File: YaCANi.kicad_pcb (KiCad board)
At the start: 2 copper layers, 20 x 50 mm, 62 parts, among them P1 SWD, P2 CAN, P3 USB, U1 STM32F042C6T6, U2 MCP2562-E/SN, U3 LD1117S33TR

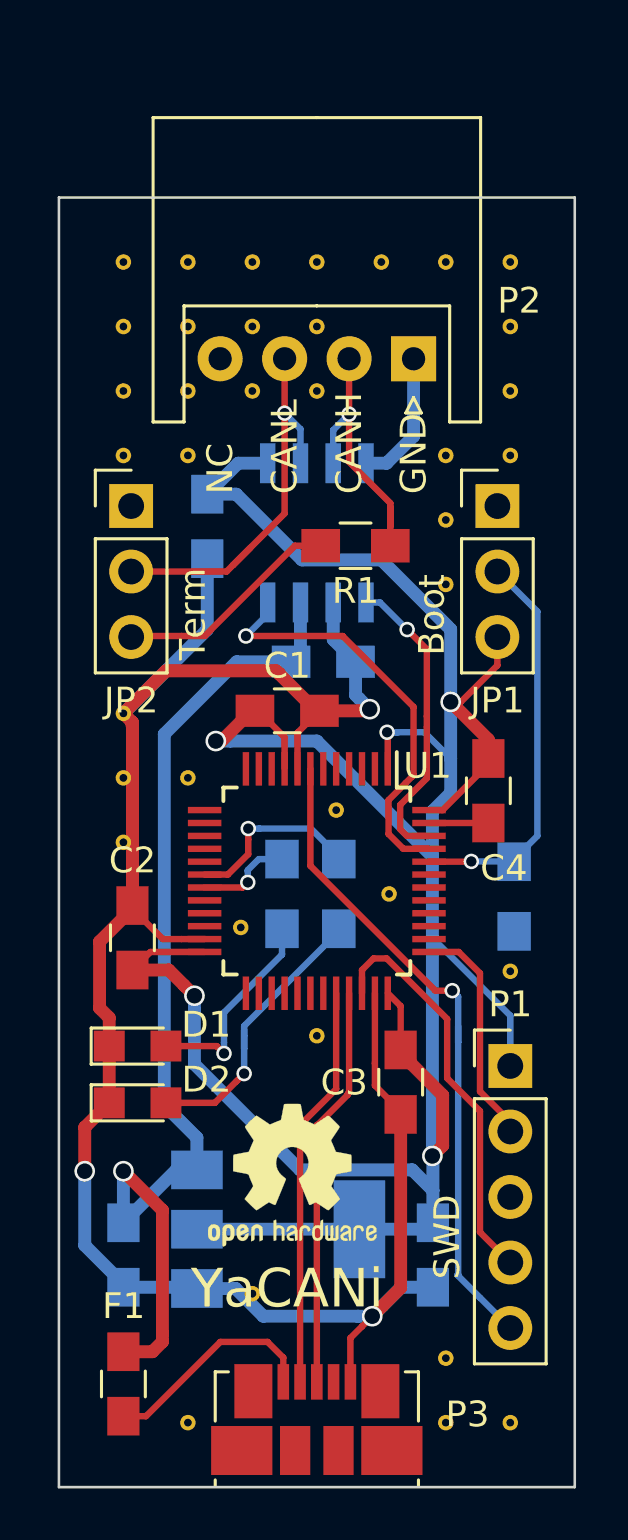
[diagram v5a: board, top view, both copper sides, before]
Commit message: add LED labelling
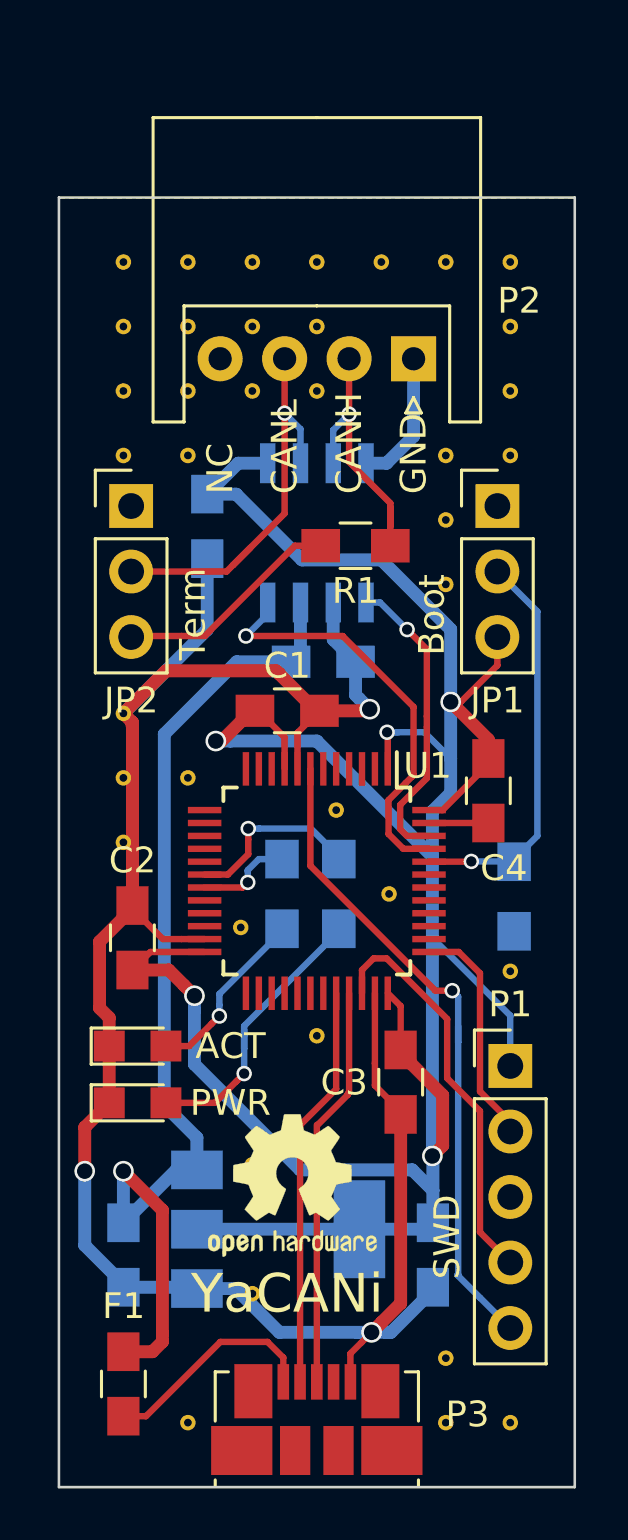
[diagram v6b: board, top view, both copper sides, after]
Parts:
- moved REF*** 0.40 mm to (130.8, 115.8)
- renumbered D1 to ACT, D2 to PWR
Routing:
- net Net-(D1-Pad2): track 8.14 -> 6.94 mm
- net GND: track 97.0 -> 97.6 mm
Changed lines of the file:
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@@
     (thickness 1.6)
     (drawings 20)
-    (tracks 280)
+    (tracks 282)
     (zones 0)
     (modules 62)
@@
     (tags "LED led 0805 SMD smd SMT smt smdled SMDLED smtled SMTLED")
     (attr smd)
-    (fp_text reference D1 (at 2.66 -0.83) (layer F.SilkS)
+    (fp_text reference ACT (at 3.6 0) (layer F.SilkS)
       (effects (font (size 1 1) (thickness 0.15)))
     )
@@
     (tags "LED led 0805 SMD smd SMT smt smdled SMDLED smtled SMTLED")
     (attr smd)
-    (fp_text reference D2 (at 2.67 -0.9) (layer F.SilkS)
+    (fp_text reference PWR (at 3.6 0) (layer F.SilkS)
       (effects (font (size 1 1) (thickness 0.15)))
     )
@@
   )
   (module Symbols:OSHW-Logo2_7.3x6mm_SilkScreen (layer F.Cu)
-    (at 130.8 115.4)
+    (at 130.8 115.8)
     (descr "Open Source Hardware Symbol")
     (tags "Logo Symbol OSHW")
@@
       (xy -0.113933 -2.757629) (xy -0.013056 -2.757714) (xy 0 -2.757714) (xy 0.10391 -2.757652)) (layer F.SilkS) (width 0.01))
   )
-  (gr_text YaCANi (at 130.6 119.8 360) (layer F.SilkS)
+  (gr_text YaCANi (at 130.6 120 360) (layer F.SilkS)
     (effects (font (size 1.5 1.5) (thickness 0.3)))
   )
@@
     (arrow2b (pts (xy 121.75 72.5) (xy 122.876504 71.913579)))
   )
+  (segment (start 136.25 119.875) (end 134.626021 121.498979) (width 0.5) (layer B.Cu) (net 1))
+  (segment (start 135 120.373239) (end 134.274259 121.09898) (width 0.5) (layer F.Cu) (net 1))
+  (segment (start 133.474261 121.898978) (end 133.87426 121.498979) (width 0.25) (layer F.Cu) (net 1))
+  (segment (start 135 113.05) (end 135 120.373239) (width 0.5) (layer F.Cu) (net 1))
+  (segment (start 133.05 122.323239) (end 133.474261 121.898978) (width 0.25) (layer F.Cu) (net 1))
+  (segment (start 133.05 123.42) (end 133.05 122.323239) (width 0.25) (layer F.Cu) (net 1))
+  (segment (start 134.439945 121.498979) (end 133.87426 121.498979) (width 0.5) (layer B.Cu) (net 1))
+  (segment (start 136.25 119.75) (end 136.25 119.875) (width 0.5) (layer B.Cu) (net 1))
+  (segment (start 134.274259 121.09898) (end 133.87426 121.498979) (width 0.5) (layer F.Cu) (net 1))
+  (segment (start 133.308575 121.498979) (end 133.87426 121.498979) (width 0.5) (layer B.Cu) (net 1))
+  (segment (start 130.298979 121.498979) (end 133.308575 121.498979) (width 0.5) (layer B.Cu) (net 1))
+  (segment (start 127.1 119.8) (end 128.6 119.8) (width 0.5) (layer B.Cu) (net 1))
+  (segment (start 134.626021 121.498979) (end 134.439945 121.498979) (width 0.5) (layer B.Cu) (net 1))
+  (via (at 133.87426 121.498979) (size 0.8) (drill 0.6) (layers F.Cu B.Cu) (net 1))
+  (segment (start 128.6 119.8) (end 130.298979 121.498979) (width 0.5) (layer B.Cu) (net 1))
   (segment (start 136.1 101.75) (end 138.4 101.75) (width 0.25) (layer F.Cu) (net 1))
   (segment (start 135.5 86.755) (end 135.5 83.75) (width 0.5) (layer B.Cu) (net 1))
@@
   (segment (start 135.5 86.755) (end 134.455 87.8) (width 0.5) (layer B.Cu) (net 1))
   (segment (start 134.455 87.8) (end 133.655 87.8) (width 0.5) (layer B.Cu) (net 1))
-  (segment (start 133.497956 121.272711) (end 133.897955 120.872712) (width 0.25) (layer F.Cu) (net 1))
-  (segment (start 133.05 121.720667) (end 133.497956 121.272711) (width 0.25) (layer F.Cu) (net 1))
-  (segment (start 133.05 123.42) (end 133.05 121.720667) (width 0.25) (layer F.Cu) (net 1))
-  (segment (start 133.33227 120.872712) (end 133.897955 120.872712) (width 0.5) (layer B.Cu) (net 1))
-  (segment (start 129.672712 120.872712) (end 133.33227 120.872712) (width 0.5) (layer B.Cu) (net 1))
-  (segment (start 128.6 119.8) (end 129.672712 120.872712) (width 0.5) (layer B.Cu) (net 1))
-  (segment (start 127.1 119.8) (end 128.6 119.8) (width 0.5) (layer B.Cu) (net 1))
-  (segment (start 134.297954 120.472713) (end 133.897955 120.872712) (width 0.5) (layer F.Cu) (net 1))
-  (segment (start 135 113.05) (end 135 119.770667) (width 0.5) (layer F.Cu) (net 1))
-  (segment (start 135 119.770667) (end 134.297954 120.472713) (width 0.5) (layer F.Cu) (net 1))
-  (segment (start 135.020667 119.75) (end 134.297954 120.472713) (width 0.5) (layer B.Cu) (net 1))
-  (segment (start 136.25 119.75) (end 135.020667 119.75) (width 0.5) (layer B.Cu) (net 1))
-  (via (at 133.897955 120.872712) (size 0.8) (drill 0.6) (layers F.Cu B.Cu) (net 1))
-  (segment (start 134.297954 120.472713) (end 133.897955 120.872712) (width 0.5) (layer B.Cu) (net 1))
   (segment (start 124.6 104.95) (end 124.6 97.957019) (width 0.5) (layer F.Cu) (net 1))
   (segment (start 124.6 97.957019) (end 124.575051 97.93207) (width 0.5) (layer F.Cu) (net 1))
@@
   (segment (start 135.239998 102.25) (end 134.980011 101.990013) (width 0.25) (layer F.Cu) (net 8))
   (segment (start 136.1 102.25) (end 135.239998 102.25) (width 0.25) (layer F.Cu) (net 8))
-  (segment (start 130.4 105.85) (end 130.4 106.85) (width 0.25) (layer B.Cu) (net 9))
-  (segment (start 130.4 106.85) (end 128.150352 109.099648) (width 0.25) (layer B.Cu) (net 9))
-  (segment (start 128.150352 109.099648) (end 128.150352 110.260771) (width 0.25) (layer B.Cu) (net 9))
-  (segment (start 128.150352 110.260771) (end 128.150352 110.685035) (width 0.25) (layer B.Cu) (net 9))
-  (segment (start 127.865317 110.4) (end 128.150352 110.685035) (width 0.25) (layer F.Cu) (net 9))
-  (segment (start 125.9 110.4) (end 127.865317 110.4) (width 0.25) (layer F.Cu) (net 9))
-  (via (at 128.150352 110.685035) (size 0.6) (drill 0.4) (layers F.Cu B.Cu) (net 9))
+  (segment (start 127.66992 109.534599) (end 127.969919 109.2346) (width 0.25) (layer F.Cu) (net 9))
+  (segment (start 126.804519 110.4) (end 127.66992 109.534599) (width 0.25) (layer F.Cu) (net 9))
+  (segment (start 127.969919 108.380081) (end 127.969919 108.810336) (width 0.25) (layer B.Cu) (net 9))
+  (segment (start 130.4 105.95) (end 127.969919 108.380081) (width 0.25) (layer B.Cu) (net 9))
+  (segment (start 130.4 105.85) (end 130.4 105.95) (width 0.25) (layer B.Cu) (net 9))
+  (segment (start 125.9 110.4) (end 126.804519 110.4) (width 0.25) (layer F.Cu) (net 9))
+  (segment (start 127.969919 108.810336) (end 127.969919 109.2346) (width 0.25) (layer B.Cu) (net 9))
+  (via (at 127.969919 109.2346) (size 0.6) (drill 0.4) (layers F.Cu B.Cu) (net 9))
   (segment (start 128.930775 111.46546) (end 128.930775 110.5) (width 0.25) (layer B.Cu) (net 10))
   (segment (start 128.930775 110.5) (end 128.930775 110) (width 0.25) (layer B.Cu) (net 10))

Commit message: add design date
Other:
- board text added: "design: 2017"
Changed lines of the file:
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@@
 (kicad_pcb (version 4) (host pcbnew 4.0.6)
   (general
-    (links 0)
+    (links 102)
     (no_connects 1)
     (area 121.699999 77.449999 141.800001 127.550001)
     (thickness 1.6)
-    (drawings 20)
+    (drawings 21)
     (tracks 282)
     (zones 0)
@@
       (xy -0.113933 -2.757629) (xy -0.013056 -2.757714) (xy 0 -2.757714) (xy 0.10391 -2.757652)) (layer F.SilkS) (width 0.01))
   )
-  (gr_text YaCANi (at 130.6 120 360) (layer F.SilkS)
+  (gr_text "design: 2017" (at 140.7 80.8 90) (layer B.SilkS)
+    (effects (font (size 0.5 0.5) (thickness 0.1)) (justify mirror))
+  )
+  (gr_text YaCANi (at 130.6 120) (layer F.SilkS)
     (effects (font (size 1.5 1.5) (thickness 0.3)))
   )
